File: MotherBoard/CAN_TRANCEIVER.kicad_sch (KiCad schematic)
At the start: 22 parts, among them U601 PTCAN1462DRQ1, U602 PTCAN1462DRQ1

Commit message: Fixed BQ79600 + minor changes
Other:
- company: (none) -> FSAE LSU
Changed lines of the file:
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@@
 	(generator_version "8.0")
 	(paper "A4")
+	(title_block
+		(date "2025-01-08")
+		(rev "A")
+		(company "FSAE LSU")
+		(comment 1 "Jacob Parent ")
+		(comment 2 "parent.jacob7@protonmail.com")
+	)
 	(junction
 		(at 139.7 118.11)

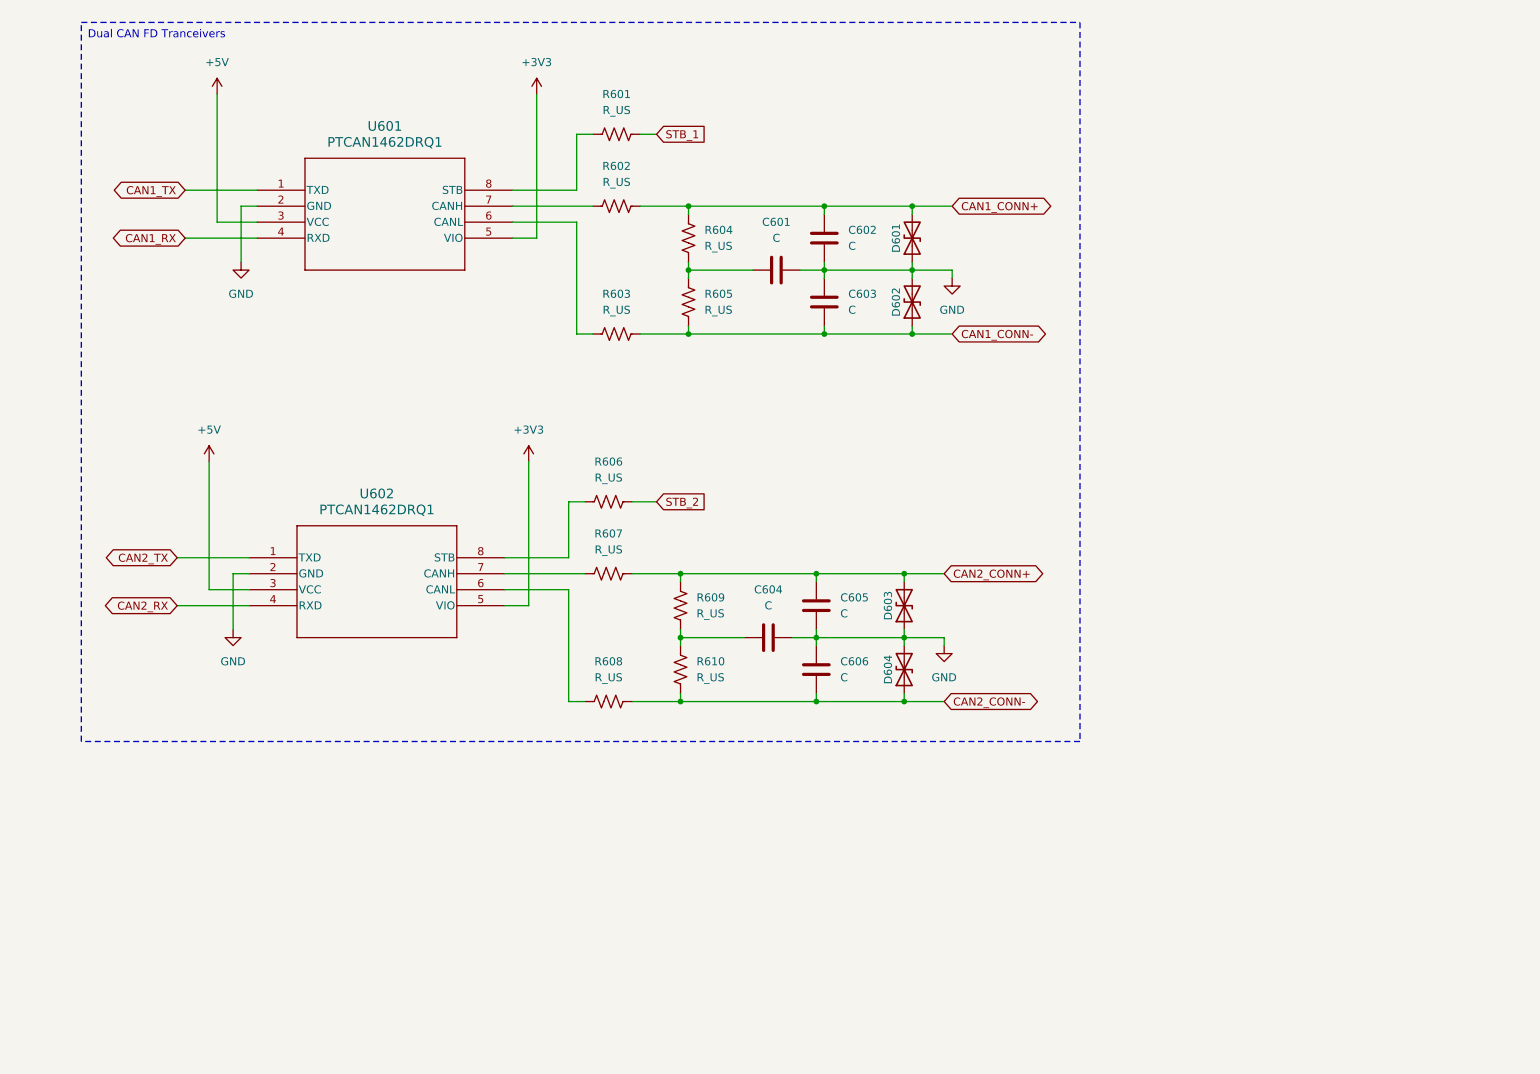
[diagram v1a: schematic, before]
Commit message: Fixed CAN tranceivers + added relay driver circuit + fixed relative file paths for 3D models + finished PSU but still need correct 3D model
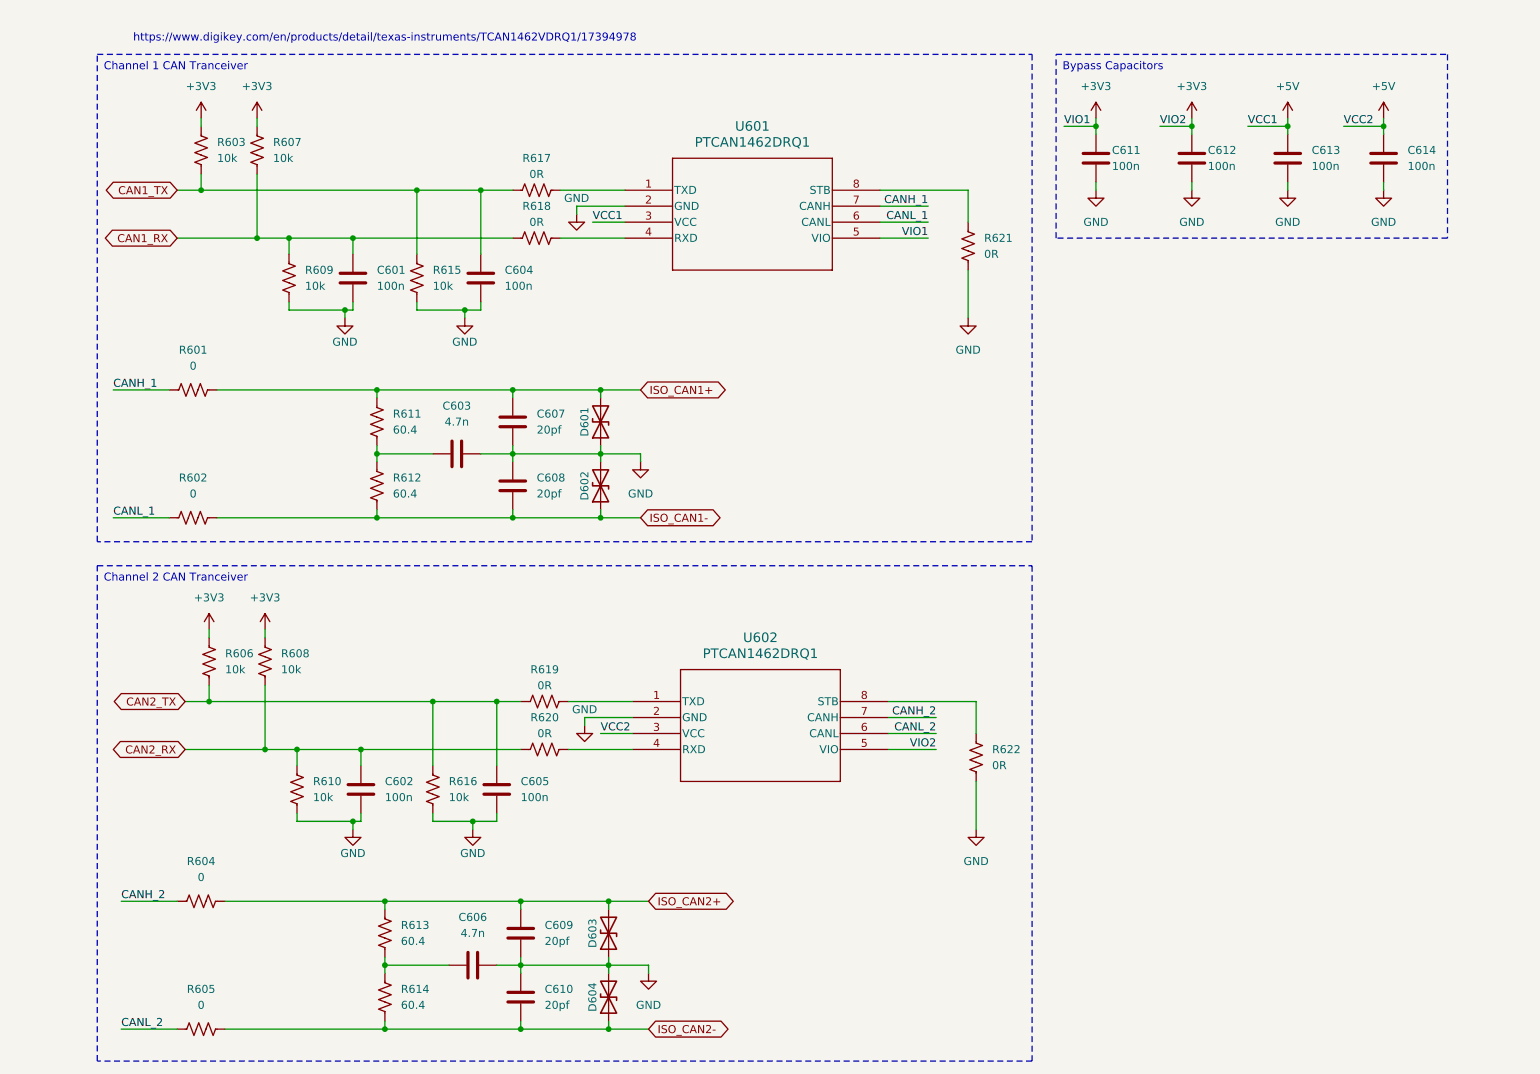
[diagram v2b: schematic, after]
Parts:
- added C601, C602, C611, C612, C613, C614: 100n, symbol Device:C
- added C609, C610: 20pf, symbol Device:C
- added R604, R605: 0, symbol Device:R_US
- added R613, R614: 60.4, symbol Device:R_US
- added R615, R616: 10k, symbol Device:R_US
- added R617, R618, R619, R620, R621, R622: 0R, symbol Device:R_US
- C603: renamed from C601; value C -> 4.7n
- C604, C605: value C -> 100n
- C606: value C -> 4.7n
- C607: renamed from C602; value C -> 20pf
- C608: renamed from C603; value C -> 20pf
- R601, R602: value R_US -> 0
- R603, R606, R607, R608, R609, R610: value R_US -> 10k
- R611: renamed from R604; value R_US -> 60.4
- R612: renamed from R605; value R_US -> 60.4
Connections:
- net STB_1 is gone; now on net CANH_1: R601.2
- net STB_2 is gone; now on net CAN2_TX: R606.2
- net +3V3: now also R603.1, R606.1, R607.1, R608.1, C611.1, C612.1
- net +5V: now also C613.1, C614.1
- net CAN1_RX: now also R607.2, R609.1, C601.2, R618.1; no longer U601.4 (RXD)
- net CAN1_TX: now also C604.2, R603.2, R615.1, R617.1; no longer U601.1 (TXD)
- net CAN2_RX: now also R608.2, R610.1, C602.2, R620.1; no longer U602.4 (RXD)
- net CAN2_TX: now also C605.2, R616.1, R619.1; no longer U602.1 (TXD)
- net GND: now also C604.1, R609.2, R610.2, C601.1, C602.1, C609.1, C610.2, C611.2, C612.2, C613.2, C614.2, R615.2, R616.2, R621.2, R622.2; no longer C604.2
- net CANL_1: now reaches U601.6 (CANL)
- net CANL_1: now also R602.2; no longer R603.1
- net CANH_1: now reaches U601.7 (CANH)
- net CANH_1: no longer R602.1
- net at U601.8 (STB): now also R621.1; no longer R601.1
- net at U602.8 (STB): now also R622.1; no longer R606.1
- net CANL_2: now reaches U602.6 (CANL)
- net CANL_2: now also R605.2; no longer R608.1
- net CANH_2: now reaches U602.7 (CANH)
- net CANH_2: now also R604.2; no longer R607.1
- net CAN1_CONN+ renamed ISO_CAN1+
- net ISO_CAN1+: now also R601.1; no longer R602.2
- net CAN1_CONN- renamed ISO_CAN1-
- net ISO_CAN1-: now also R602.1; no longer R603.2
- removed net CAN2_CONN+: C605.2, D603.2 (A2), R607.2, R609.2
- removed net CAN2_CONN-: C606.1, D604.1 (A1), R608.2, R610.1
- new net: R617.2, U601.1 (TXD)
- new net: R618.2, U601.4 (RXD)
- new net: R619.2, U602.1 (TXD)
- new net: R620.2, U602.4 (RXD)
- new net: C606.1, R613.1, R614.2
- new net ISO_CAN2+: C609.2, D603.2 (A2), R604.1, R613.2
- new net ISO_CAN2-: C610.1, D604.1 (A1), R605.1, R614.1
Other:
- note added: "https://www.digikey.com/en/products/detail/texas-instruments/TCAN1462VDRQ1/17394978"
- moved on the sheet: C603, C607, C608, D601, D602, R611, R612, U601

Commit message: Revised all schematics + completed relay driver page
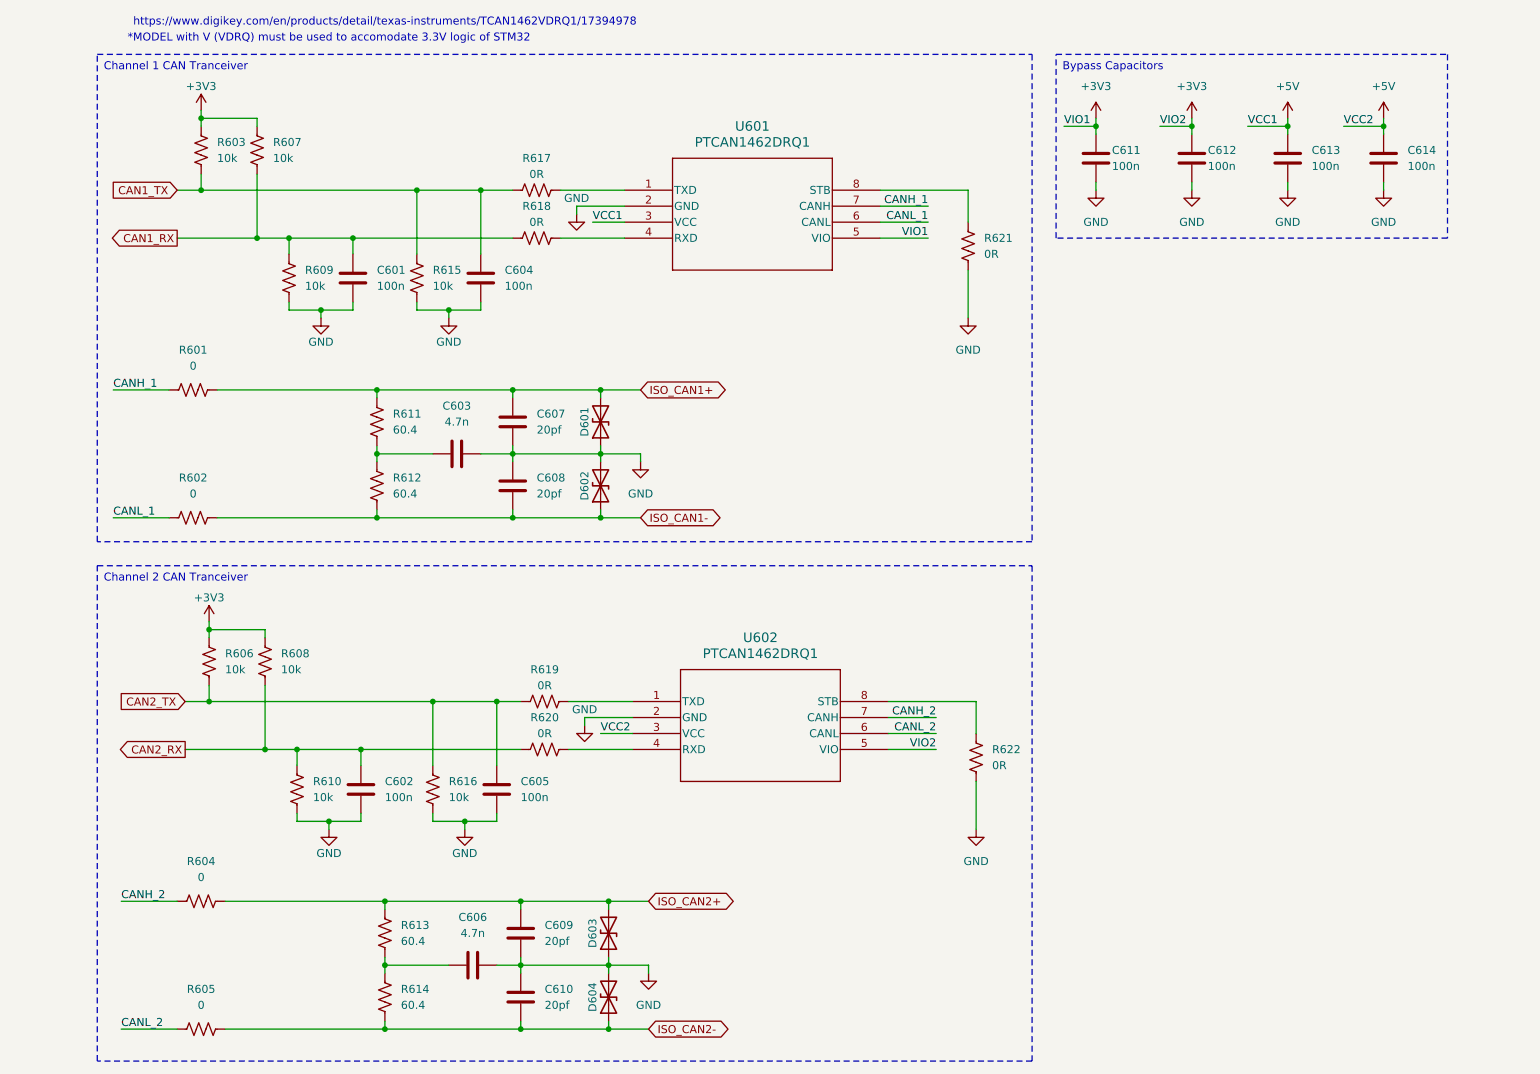
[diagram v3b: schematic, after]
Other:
- note added: "*MODEL with V (VDRQ) must be used to accomodate 3.3V logic of STM32"

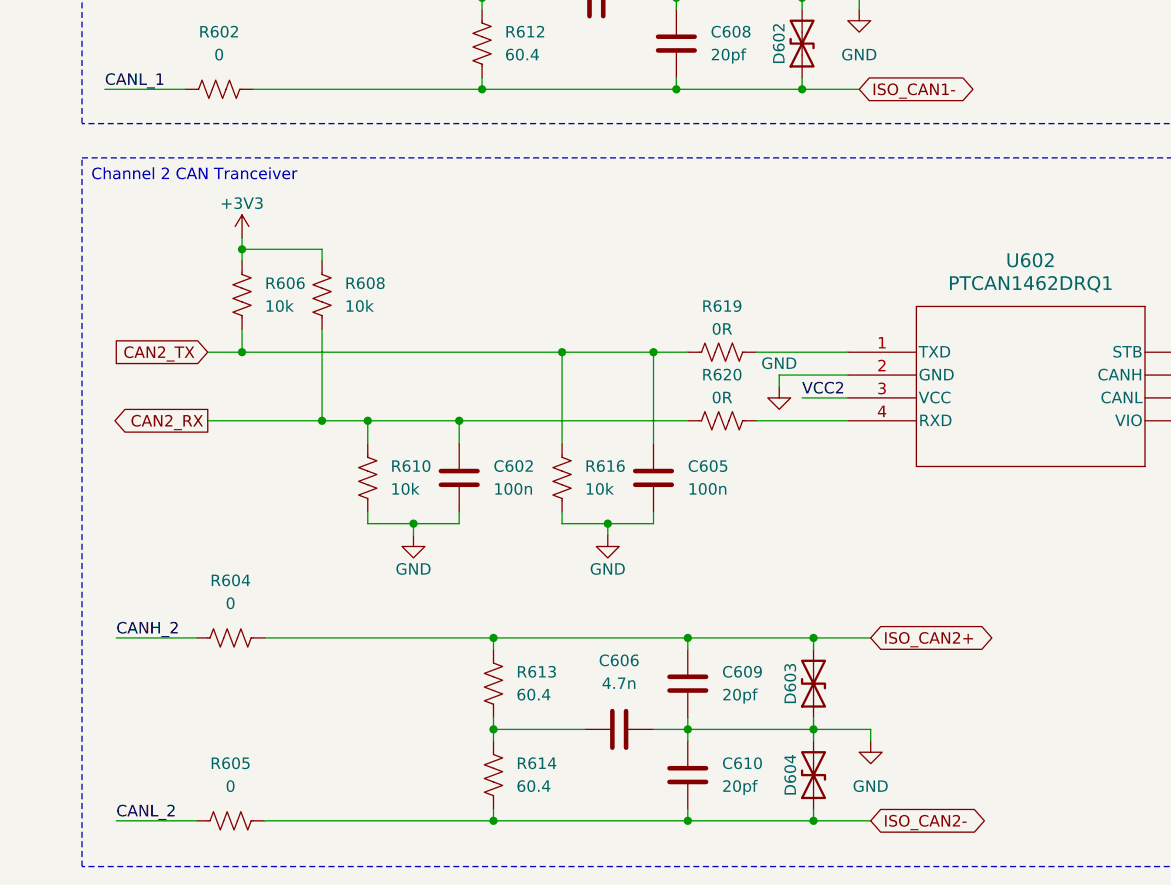
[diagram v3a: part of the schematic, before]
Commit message: Fixed 3D model paths. Finished PSU ORing shcematic.
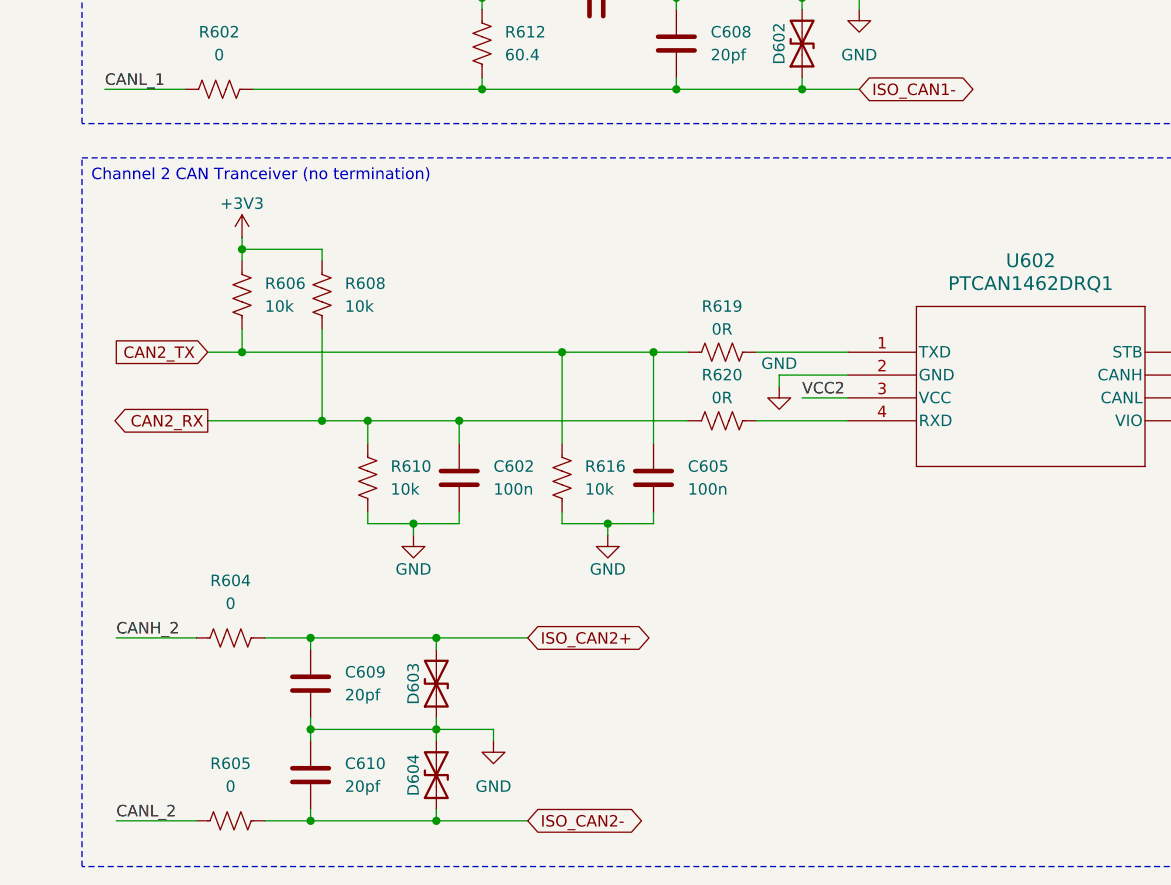
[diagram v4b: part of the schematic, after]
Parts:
- removed C606: 4.7n, symbol Device:C
- removed R613, R614: 60.4, symbol Device:R_US
- removed U601, U602: PTCAN1462DRQ1, TCAN:TCAN, symbol TCAN1462:PTCAN1462DRQ1
- added U601, U602: PTCAN1462DRQ1, CAN1462:CAN1462, symbol TCAN:PTCAN1462DRQ1
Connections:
- net +3V3: now also U601.5 (VIO), U602.5 (VIO)
- net +5V: now also U601.3 (VCC), U602.3 (VCC)
- net CANH_1: now also U601.7 (CANH)
- net CANH_2: now also U602.7 (CANH)
- net CANL_1: now also U601.6 (CANL)
- net CANL_2: now also U602.6 (CANL)
- net GND: now also U601.2 (GND), U602.2 (GND)
- net at R617.2: now also U601.1 (TXD)
- net at R618.2: now also U601.4 (RXD)
- net at R621.1: now also U601.8 (STB)
- net at R619.2: now also U602.1 (TXD)
- net at R620.2: now also U602.4 (RXD)
- net at R622.1: now also U602.8 (STB)
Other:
- moved on the sheet: C609, C610, D603, D604
